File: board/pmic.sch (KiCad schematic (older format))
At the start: 59 parts, among them J11 DB9, J12 RJ45, P48 CONN_6, P50 CONN_16X2, P51 CONN_4, U17 MAX4377, U18 MAX4378, U19 PIC18F85J94, U20 MAX3227, U21 MAX3490, X2 CRYSTAL

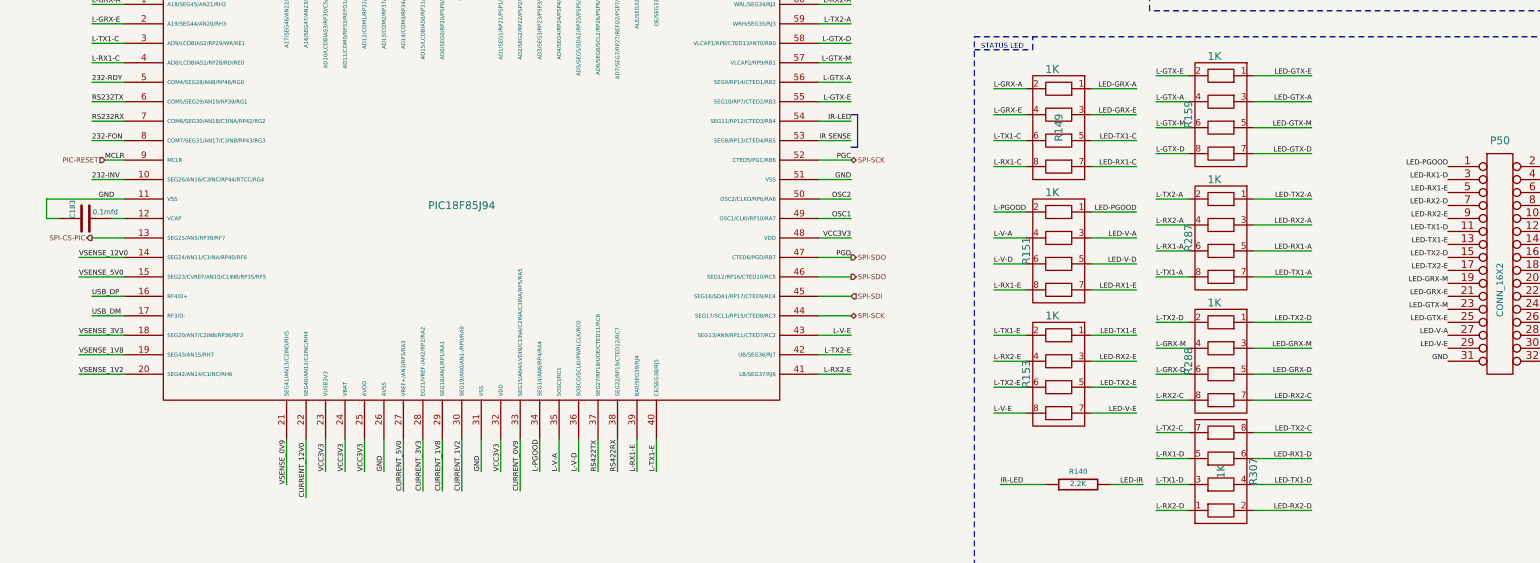
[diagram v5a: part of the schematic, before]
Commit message: Issue #1027 - Schematics final changes.
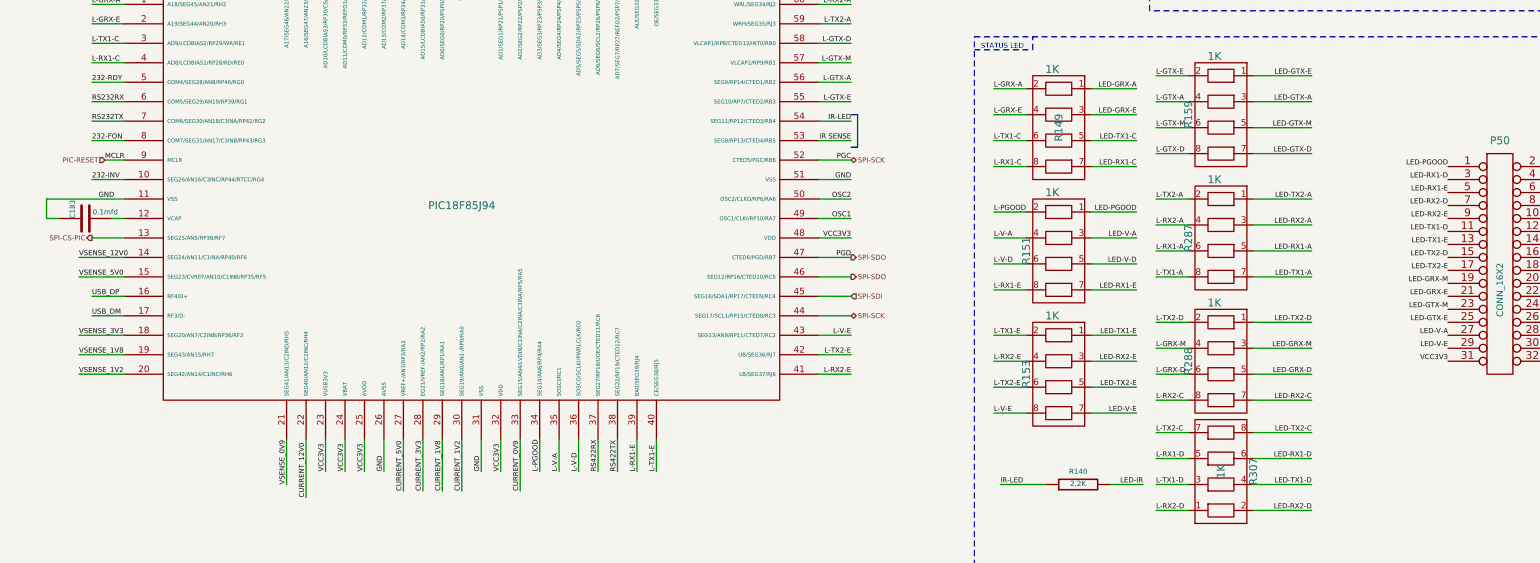
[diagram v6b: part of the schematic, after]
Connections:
- net GND: no longer P50.31 (P31)
- net RS232RX: now also U19.6 (COM5/SEG29/AN19/RP39/RG1); no longer U19.7 (COM6/SEG30/AN18/C3INA/RP42/RG2)
- net RS232TX: now also U19.7 (COM6/SEG30/AN18/C3INA/RP42/RG2); no longer U19.6 (COM5/SEG29/AN19/RP39/RG1)
- net RS422RX: now also U19.37 (SEG27/RP18/UOE/CTED11/RC6); no longer U19.38 (SEG22/RP19/CTED12/RC7)
- net RS422TX: now also U19.38 (SEG22/RP19/CTED12/RC7); no longer U19.37 (SEG27/RP18/UOE/CTED11/RC6)
- net VCC3V3: now also P50.31 (P31)
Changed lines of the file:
@@
 Sheet 7 8
 Title "HDMI2USB"
-Date "16 apr 2014"
+Date "17 apr 2014"
 Rev ""
 Comp ""
@@
 Text Label 9250 7000 2    39   ~ 0
 OSC2
+Text Label 3400 6400 0    39   ~ 0
+RS232TX
 Text Label 3400 6250 0    39   ~ 0
-RS232TX
-Text Label 3400 6400 0    39   ~ 0
 RS232RX
+Text Label 7450 9100 1    39   ~ 0
+RS422TX
 Text Label 7300 9100 1    39   ~ 0
-RS422TX
-Text Label 7450 9100 1    39   ~ 0
 RS422RX
 Text HLabel 9250 7600 2    39   Output ~ 0
@@
 Text Label 14650 8250 0    39   ~ 0
 GND
-Text Label 13850 8250 2    39   ~ 0
-GND
 Text Label 11500 9200 2    39   ~ 0
 LED-IR
@@
 Wire Wire Line
 	5250 1900 5600 1900
+Text Label 13850 8250 2    39   ~ 0
+VCC3V3
 $EndSCHEMATC

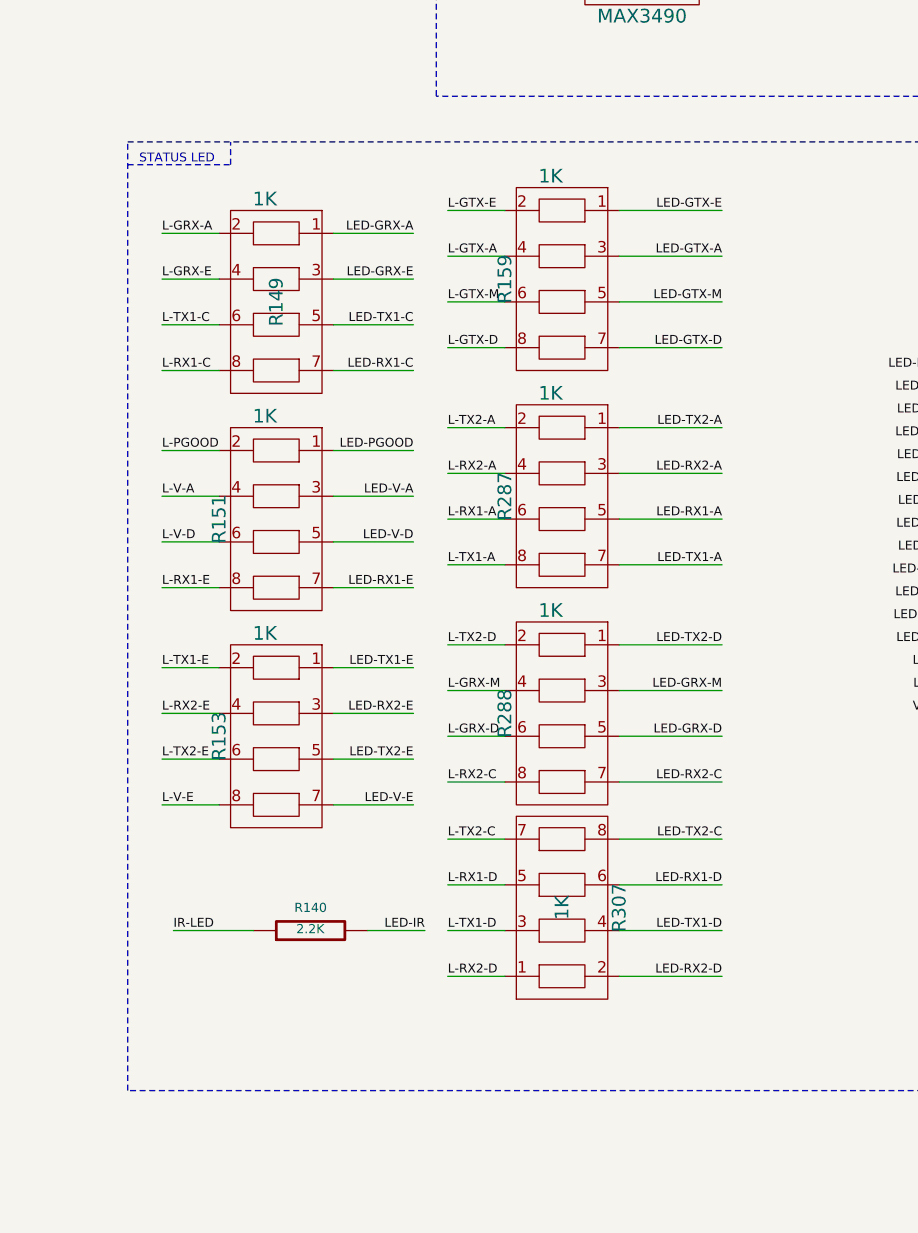
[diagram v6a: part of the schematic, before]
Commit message: Issue #1053 - Cypress routing
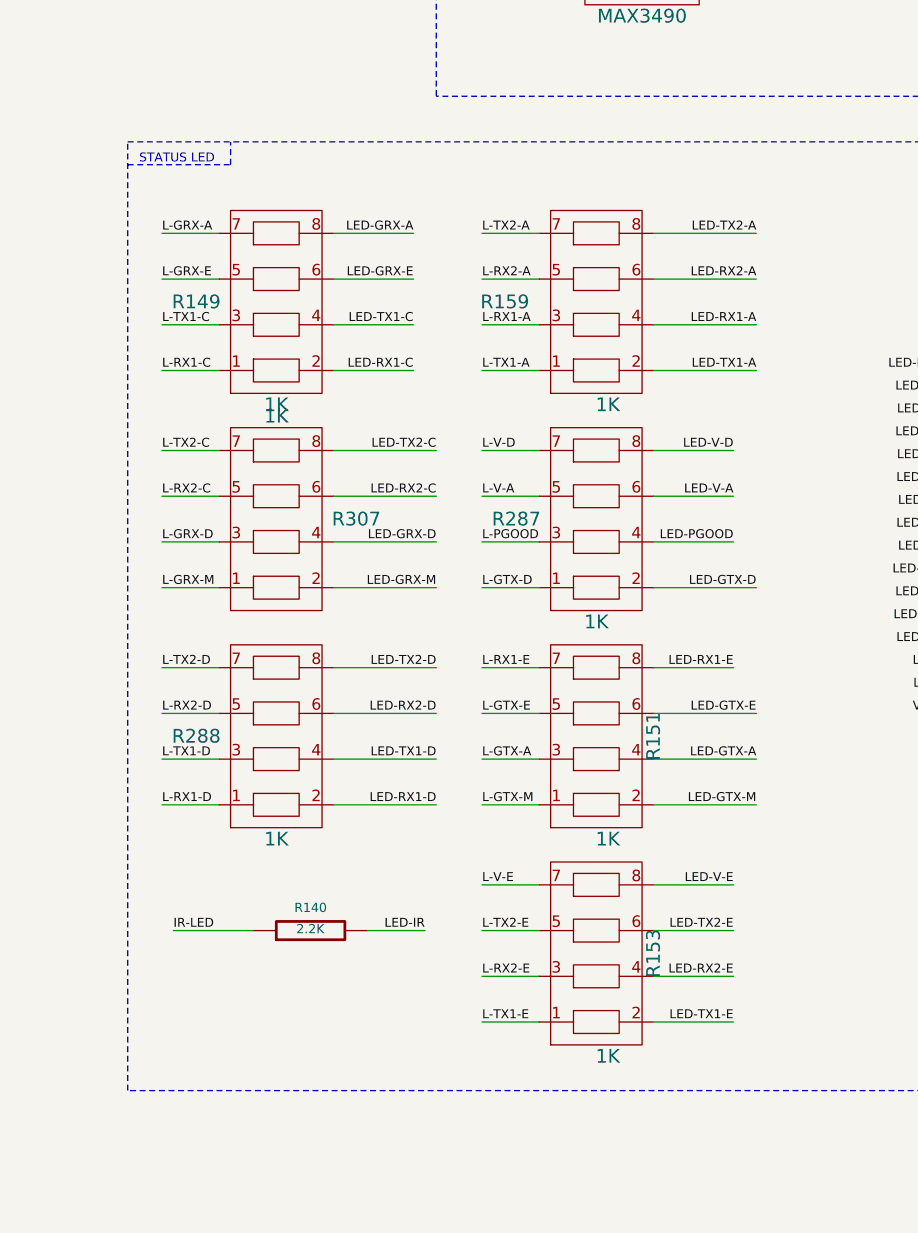
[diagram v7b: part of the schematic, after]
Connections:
- net L-GRX-A: now also R149.7; no longer R149.2
- net L-GRX-D: now also R307.3; no longer R288.6
- net L-GRX-E: now also R149.5; no longer R149.4
- net L-GRX-M: now also R307.1; no longer R288.4
- net L-GTX-A: now also R151.3; no longer R159.4
- net L-GTX-D: now also R287.1; no longer R159.8
- net L-GTX-E: now also R151.5; no longer R159.2
- net L-GTX-M: now also R151.1; no longer R159.6
- net L-PGOOD: now also R287.3; no longer R151.2
- net L-RX1-A: now also R159.3; no longer R287.6
- net L-RX1-C: now also R149.1; no longer R149.8
- net L-RX1-D: now also R288.1; no longer R307.5
- net L-RX1-E: now also R151.7; no longer R151.8
- net L-RX2-A: now also R159.5; no longer R287.4
- net L-RX2-C: now also R307.5; no longer R288.8
- net L-RX2-D: now also R288.5; no longer R307.1
- net L-RX2-E: now also R153.3; no longer R153.4
- net L-TX1-A: now also R159.1; no longer R287.8
- net L-TX1-C: now also R149.3; no longer R149.6
- net L-TX1-D: now also R288.3; no longer R307.3
- net L-TX1-E: now also R153.1; no longer R153.2
- net L-TX2-A: now also R159.7; no longer R287.2
- net L-TX2-D: now also R288.7; no longer R288.2
- net L-TX2-E: now also R153.5; no longer R153.6
- net L-V-A: now also R287.5; no longer R151.4
- net L-V-D: now also R287.7; no longer R151.6
- net L-V-E: now also R153.7; no longer R153.8
- net LED-GRX-A: now also R149.8; no longer R149.1
- net LED-GRX-D: now also R307.4; no longer R288.5
- net LED-GRX-E: now also R149.6; no longer R149.3
- net LED-GRX-M: now also R307.2; no longer R288.3
- net LED-GTX-A: now also R151.4; no longer R159.3
- net LED-GTX-D: now also R287.2; no longer R159.7
- net LED-GTX-E: now also R151.6; no longer R159.1
- net LED-GTX-M: now also R151.2; no longer R159.5
- net LED-PGOOD: now also R287.4; no longer R151.1
- net LED-RX1-A: now also R159.4; no longer R287.5
- net LED-RX1-C: now also R149.2; no longer R149.7
- net LED-RX1-D: now also R288.2; no longer R307.6
- net LED-RX1-E: now also R151.8; no longer R151.7
- net LED-RX2-A: now also R159.6; no longer R287.3
- net LED-RX2-C: now also R307.6; no longer R288.7
- net LED-RX2-D: now also R288.6; no longer R307.2
- net LED-RX2-E: now also R153.4; no longer R153.3
- net LED-TX1-A: now also R159.2; no longer R287.7
- net LED-TX1-C: now also R149.4; no longer R149.5
- net LED-TX1-D: now also R288.4; no longer R307.4
- net LED-TX1-E: now also R153.2; no longer R153.1
- net LED-TX2-A: now also R159.8; no longer R287.1
- net LED-TX2-D: now also R288.8; no longer R288.1
- net LED-TX2-E: now also R153.6; no longer R153.5
- net LED-V-A: now also R287.6; no longer R151.3
- net LED-V-D: now also R287.8; no longer R151.5
- net LED-V-E: now also R153.8; no longer R153.7
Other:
- moved on the sheet: R151, R153, R159, R287, R288, R307
